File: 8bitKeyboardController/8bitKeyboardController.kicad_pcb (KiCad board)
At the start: 2 copper layers, 43.5 x 70 mm, 10 parts

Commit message: PCB 1st routing
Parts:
- added G***: LOGO, LOGO, B.Cu at (152.5, 83.5)
- added HOLE-BOTTOMLEFT: MountingHole_3.2mm_M3, MountingHole:MountingHole_3.2mm_M3, F.Cu at (122.5, 116.0)
- added HOLE-BOTTOMRIGHT: MountingHole_3.2mm_M3, MountingHole:MountingHole_3.2mm_M3, F.Cu at (165.0, 116.0)
- added HOLE-TOPLEFT: MountingHole_3.2mm_M3, MountingHole:MountingHole_3.2mm_M3, F.Cu at (122.5, 55.0)
- added HOLE-TOPRIGHT: MountingHole_3.2mm_M3, MountingHole:MountingHole_3.2mm_M3, F.Cu at (165.0, 55.0)
- moved LEDS(opt)1 61.5 mm to (122.0, 63.0)
- moved PS2 43.3 mm to (121.0, 95.0)
- moved RCAPS1 31.6 mm to (125.0, 79.0), turned to -90 degrees
- moved RNUM1 28.7 mm to (121.0, 79.0), turned to -90 degrees
- moved PS/2 19.0 mm to (146.7, 115.5)
- moved RSCROLL1 15.2 mm to (125.0, 99.0), turned to -90 degrees
- moved C16 9.38 mm to (160.5, 61.5)
- moved C64 8.84 mm to (154.0, 61.5)
- moved LVL1 3.05 mm to (141.7, 118.7), turned to 180 degrees
- moved Raspberry_Pi_Pico1 1.50 mm to (138.8, 77.0)
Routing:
- net Net-(C64-Pin_1): track 0.00 -> 183.4 mm
- net Net-(C16-Pin_18): track 0.00 -> 87.9 mm
- net Net-(C64-Pin_4): track 0.00 -> 82.7 mm
- net Net-(C16-Pin_17): track 0.00 -> 66.4 mm
- net Net-(C16-Pin_3): track 0.00 -> 65.8 mm
- net Net-(LVL1-LV): track 0.00 -> 61.9 mm
- net Net-(C16-Pin_7): track 0.00 -> 61.2 mm
- net Net-(C16-Pin_9): track 0.00 -> 58.7 mm
- net Net-(C16-Pin_15): track 0.00 -> 58.2 mm
- net Net-(C16-Pin_6): track 0.00 -> 57.2 mm
- net Net-(C16-Pin_14): track 0.00 -> 56.8 mm
- net Net-(C16-Pin_19): track 0.00 -> 56.3 mm
- net Net-(C64-Pin_3): track 0.00 -> 52.7 mm
- net Net-(C16-Pin_10): track 0.00 -> 51.0 mm
- net Net-(C16-Pin_1): track 0.00 -> 45.5 mm, vias 0 -> 1
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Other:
- board size 43.5 x 70 mm -> 50.5 x 70.5 mm
- board text added: "(opt)LEDs"
- board text added: "2026/09/24"
- board text added: "3.3V LOW side"
- board text added: "C16/C64 Keyboard QMK/VIAL USB PS/2"
- board text added: "C16/C64 QMK/VIAL Keyboard Controller PCB"
- board text added: "C16/C64 QMK/VIAL USB PS/2 keyboard"
- board text added: "CAPS+ SCRL+ NUM+"
- board text added: "DATA GND +5V CLK"
- board text added: "Geeky keyboard controller board"
- board text added: "Keyboard Connector - to match firmware"
- board text added: "wereallgeeks.wordpress.com"
- board text removed: "3.3V LOW SIDE"
- board text removed: "8bit keyboard controller QMK/VIAL wereallgeeks.wordpress.com"
- board text removed: "CAP+ SCRL+ NUM+"
- board text removed: "DAT XXX GND +5V CLK XXX"
- board text removed: "SCRL-CAPS-NUM"

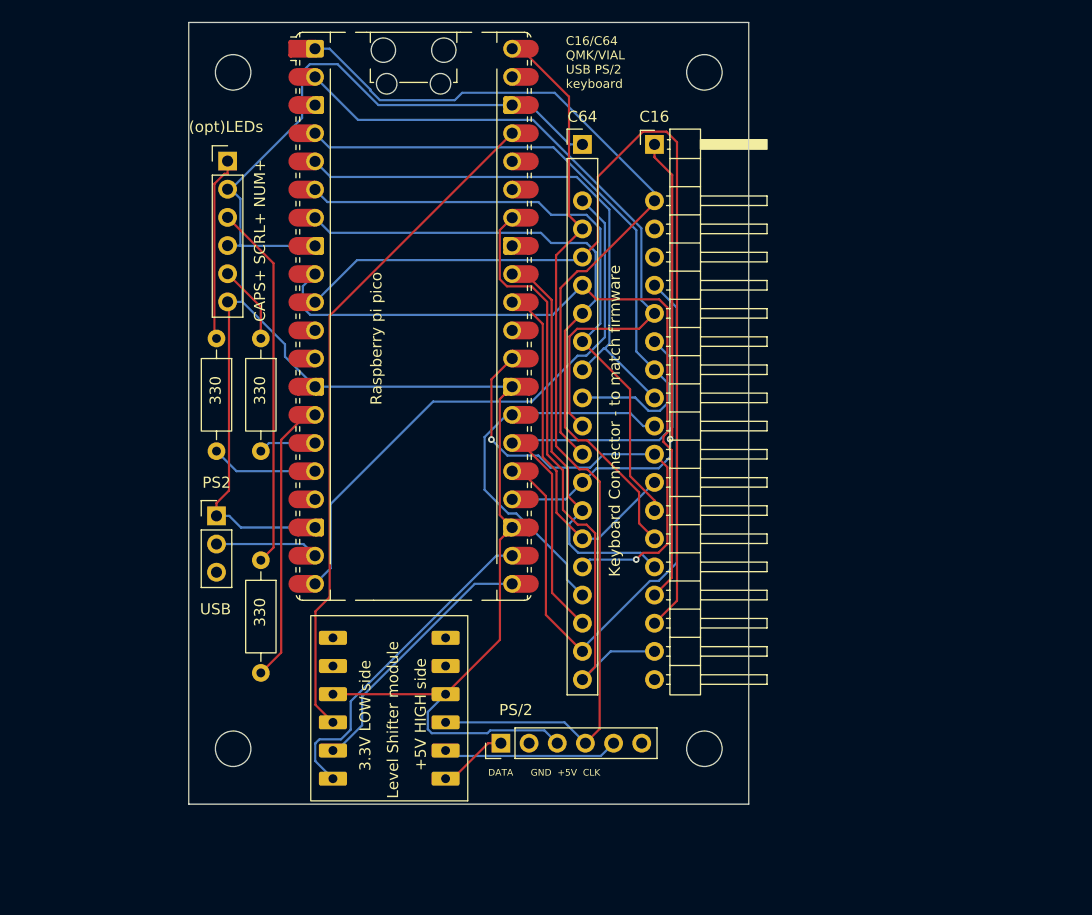
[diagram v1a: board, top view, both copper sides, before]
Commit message: Shaped to fit on mechboard
Positionned connector to be (hopefully) able to solder on top (bottom?) of Mechboard. mounting hole to position spacer.
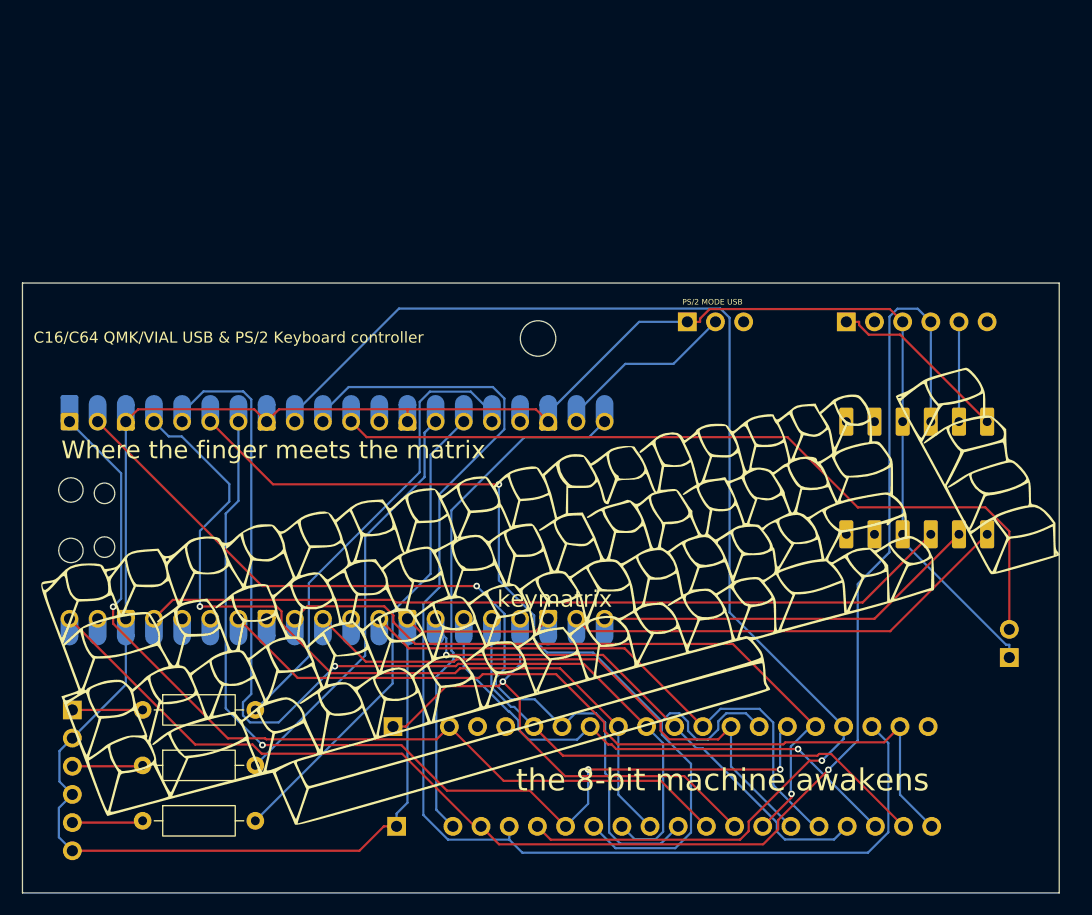
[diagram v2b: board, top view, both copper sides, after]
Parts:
- removed G***: LOGO, LOGO
- removed HOLE-BOTTOMRIGHT, HOLE-TOPLEFT, HOLE-TOPRIGHT: MountingHole_3.2mm_M3, MountingHole:MountingHole_3.2mm_M3
- removed LEDS(opt)1: LEDS 6 pin connector, Connector_PinHeader_2.54mm:PinHeader_1x06_P2.54mm_Vertical
- removed LVL1: ~, 8bitLibrary:Level Shifter - TroughHole
- removed PS/2: PS/2 6pin connector, Connector_PinHeader_2.54mm:PinHeader_1x06_P2.54mm_Vertical
- removed PS2: Mode 3pin switch, Connector_PinHeader_2.54mm:PinHeader_1x03_P2.54mm_Vertical
- added CAPS_SWT_C64: Conn_01x02_Pin, 8bitLibrary:ExtraSwitchConnector-2pin, B.Cu at (192.5, 107.8)
- added Geek: LOGO, LOGO, B.Cu at (173.0, 107.0)
- added LEDS(opt)3: LEDS 6 pin connector, 8bitLibrary:LedConnector_6pin, B.Cu at (108.0, 112.5)
- added Level-Shifter-1: ~, 8bitLibrary:Level Shifter - TroughHole, B.Cu at (177.8, 86.5)
- added MODE: Mode 3pin switch, 8bitLibrary:ModeSwitch-3pin, B.Cu at (163.5, 77.5)
- added keymatrix: LOGO, LOGO, F.Cu at (151.5, 102.5)
- added port-PS/2: PS/2 6pin connector, 8bitLibrary:PS2_Connector-6pin, B.Cu at (177.8, 77.5)
- C16: footprint 8bitLibrary:8BitKeyboardConnector_Horizontal -> 8bitLibrary:8bitKeyboardConnector_Vertical; moved to B.Cu
- C64, Raspberry_Pi_Pico1: moved to B.Cu
- moved C64 63.7 mm to (137.2, 123.0), turned to -90 degrees
- moved C16 57.6 mm to (136.9, 114.0), turned to -90 degrees
- moved HOLE-BOTTOMLEFT 46.1 mm to (150.0, 79.0)
- moved RCAPS1 44.8 mm to (114.3, 122.5), turned to 0 degrees
- moved RNUM1 34.2 mm to (114.3, 112.5), turned to 0 degrees
- moved RSCROLL1 21.4 mm to (114.3, 117.5), turned to 0 degrees
- moved Raspberry_Pi_Pico1 19.6 mm to (131.9, 95.4), turned to -90 degrees
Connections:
- Raspberry_Pi_Pico1 pad 11: unconnected-(Raspberry_Pi_Pico1-GPIO8-Pad11) -> Net-(CAPS_SWT_C64-Pin_2)
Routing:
- net Net-(CAPS_SWT_C64-Pin_2): track 0.00 -> 73.1 mm
- net Net-(C64-Pin_4): track 82.7 -> 137.6 mm, vias 0 -> 1
- net Net-(C16-Pin_17): track 66.4 -> 118.9 mm, vias 0 -> 1
- net Net-(C16-Pin_10): track 51.0 -> 92.7 mm, vias 0 -> 1
- net Net-(Raspberry_Pi_Pico1-GPIO11): track 5.99 -> 44.6 mm
- net Net-(C64-Pin_1): track 183.4 -> 221.6 mm
- net Net-(C16-Pin_14): track 56.8 -> 92.8 mm, vias 0 -> 1
- net Net-(Raspberry_Pi_Pico1-GPIO12): track 10.4 -> 42.4 mm
- net Net-(C16-Pin_15): track 58.2 -> 89.6 mm, vias 0 -> 3
- net Net-(C16-Pin_16): track 36.7 -> 64.3 mm, vias 0 -> 1
- net Net-(LEDS(opt)3-Pin_3): track 33.1 -> 6.37 mm
- net Net-(C16-Pin_18): track 87.9 -> 114.6 mm
- net Net-(C16-Pin_13): track 33.0 -> 54.4 mm
- net Net-(C16-Pin_19): track 56.3 -> 76.7 mm
- net Net-(C16-Pin_7): track 61.2 -> 81.0 mm, vias 0 -> 1
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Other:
- board size 50.5 x 70.5 mm -> 93.5 x 55 mm
- board text added: "C16/C64 QMK/VIAL USB & PS/2 Keyboard controller"
- board text added: "Keyboard Connector - to match firmware C H O O S E W I S E L Y"
- board text added: "Let's build"
- board text added: "PS/2 MODE USB"
- board text added: "Where the finger meets the matrix"
- board text added: "eeky things"
- board text added: "the 8-bit machine awakens"
- board text removed: "(opt)LEDs"
- board text removed: "+5V HIGH side"
- board text removed: "3.3V LOW side"
- board text removed: "330"
- board text removed: "C16/C64 QMK/VIAL USB PS/2 keyboard"
- board text removed: "CAPS+ SCRL+ NUM+"
- board text removed: "DATA GND +5V CLK"
- board text removed: "Keyboard Connector - to match firmware"
- board text removed: "Level Shifter module"
- board text removed: "Raspberry pi pico"
- board text removed: "USB"

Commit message: minor revisions
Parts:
- RCAPS1, RNUM1, RSCROLL1: moved to B.Cu
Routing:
- net Net-(CAPS_SWT_C64-Pin_2): track 73.1 -> 74.2 mm

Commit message: visual update
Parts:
- moved keymatrix 0.50 mm to (151.0, 102.5)
